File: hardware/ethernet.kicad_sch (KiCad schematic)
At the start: 25 parts, among them J4 HC-RJ45-055-7, U2 TMI7301, U5 SI3404-A-GMR

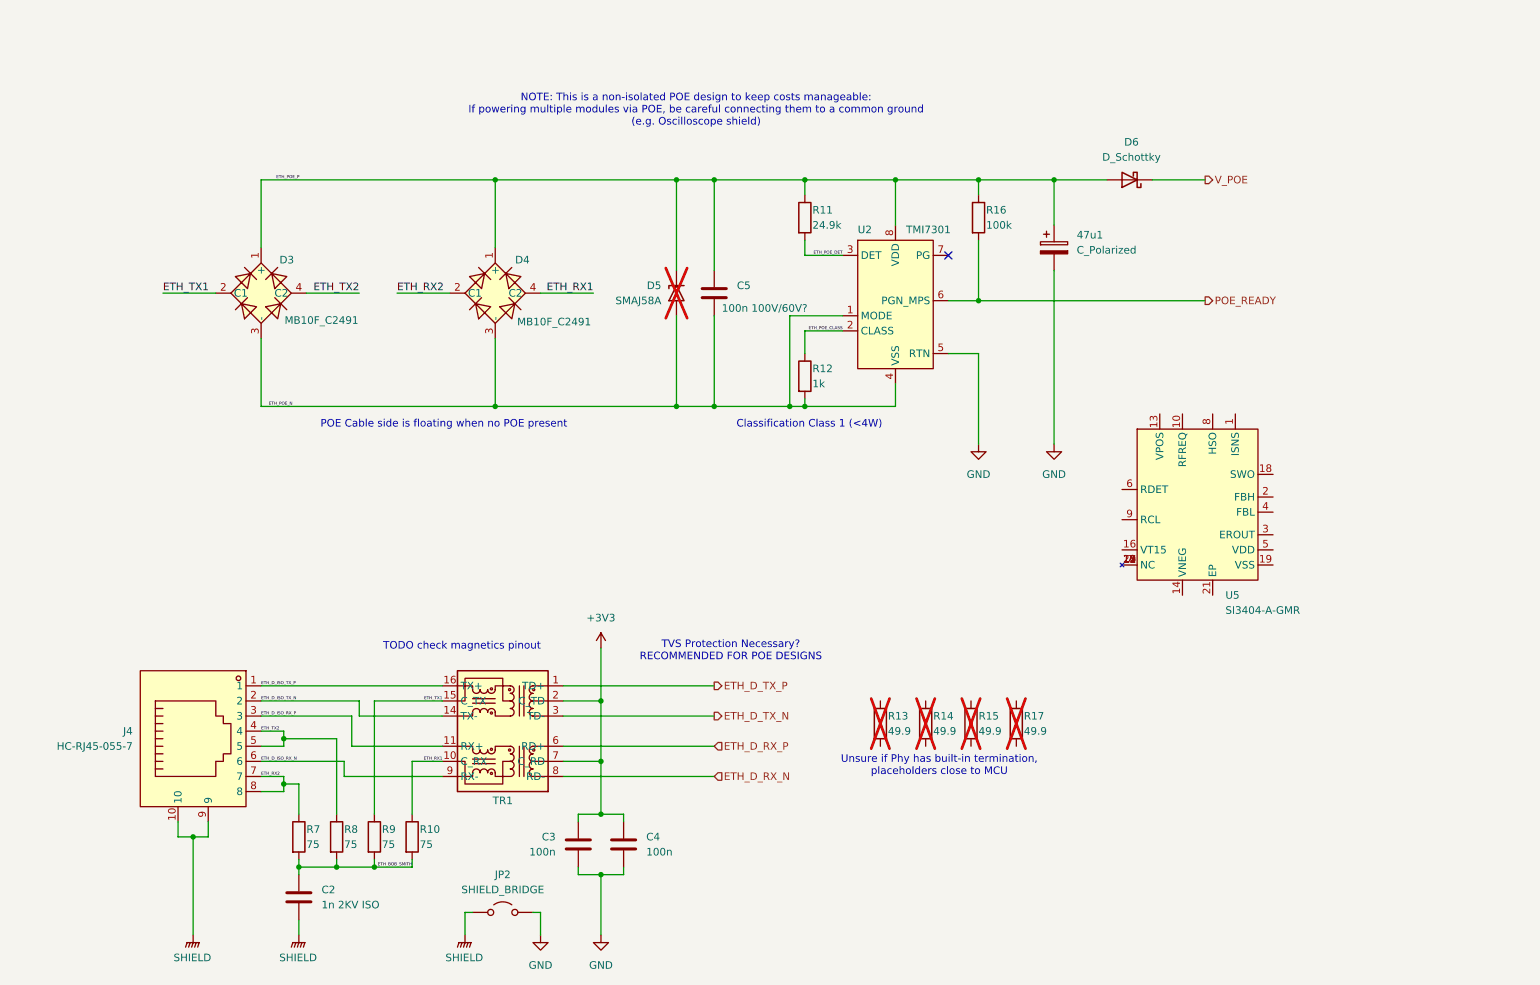
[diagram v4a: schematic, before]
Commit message: Add XTAL, rough POE Schematic
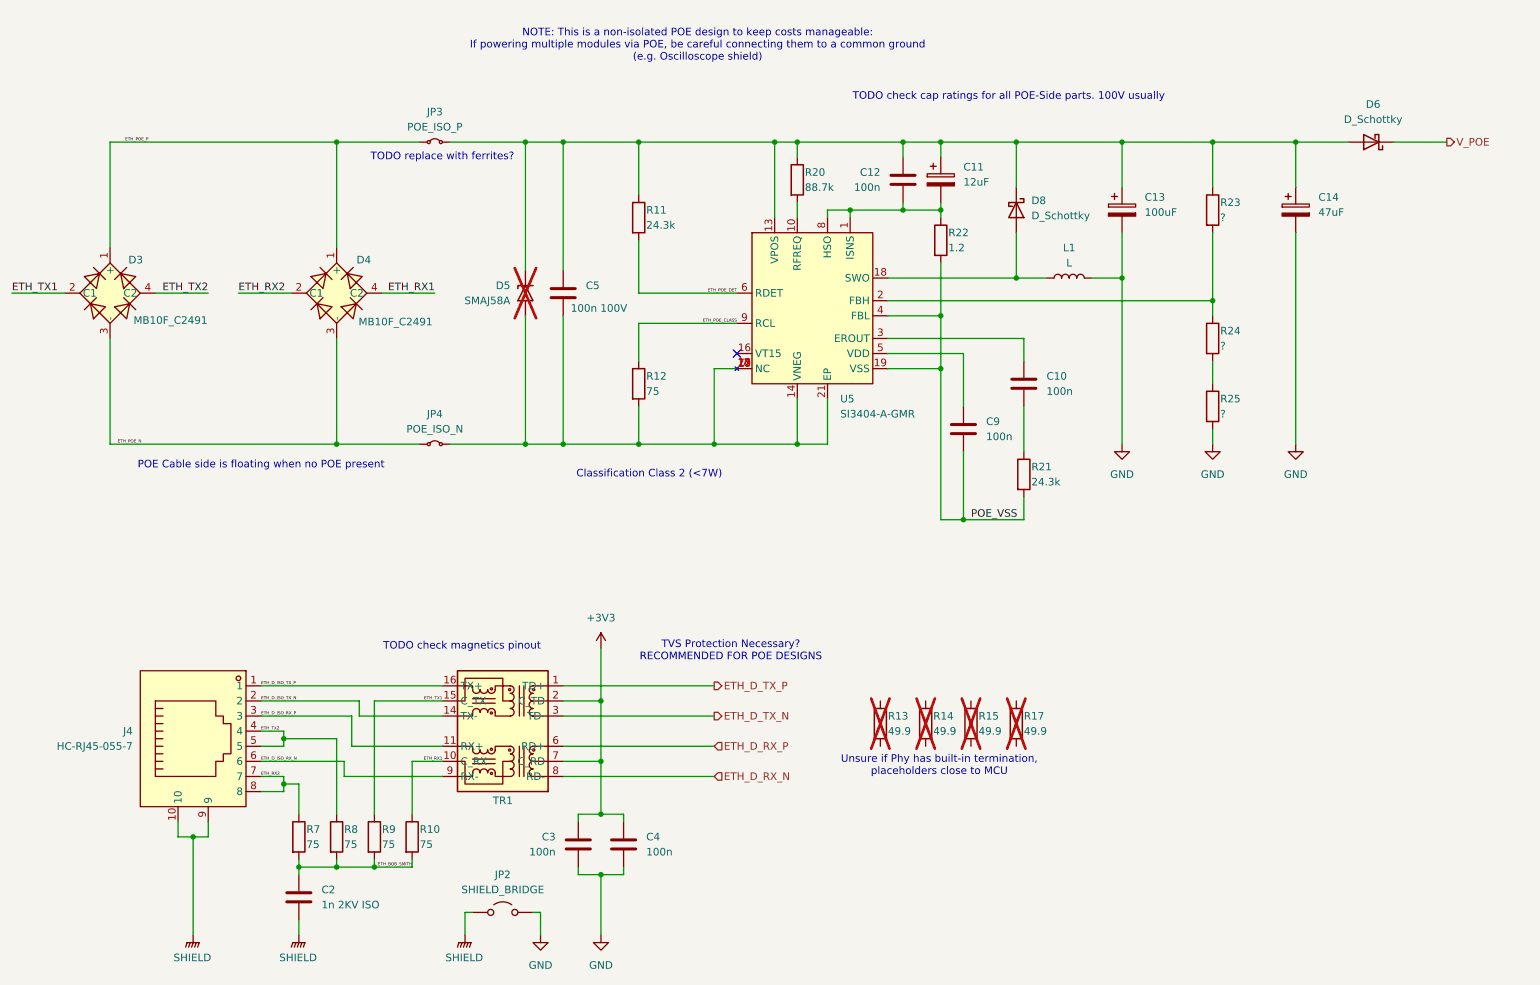
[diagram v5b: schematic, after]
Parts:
- removed R16: 100k, Resistor_SMD:R_0402_1005Metric, symbol Device:R
- removed U2: TMI7301, uPTP:SOP-8_L4.9-W3.9-P1.27-LS6.0-TL, symbol uPTP:TMI7301
- added C10, C12, C9: 100n, Capacitor_SMD:C_0402_1005Metric, symbol Device:C
- added C11: 12uF, symbol Device:C_Polarized
- added C13: 100uF, symbol Device:C_Polarized
- added D8: D_Schottky, symbol Device:D_Schottky
- added JP3: POE_ISO_P, symbol Jumper:Jumper_2_Small_Bridged
- added JP4: POE_ISO_N, symbol Jumper:Jumper_2_Small_Bridged
- added L1: L, symbol Device:L
- added R20: 88.7k, Resistor_SMD:R_0402_1005Metric, symbol Device:R
- added R21: 24.3k, Resistor_SMD:R_0402_1005Metric, symbol Device:R
- added R22: 1.2, Resistor_SMD:R_0402_1005Metric, symbol Device:R
- added R23, R24, R25: ?, Resistor_SMD:R_0402_1005Metric, symbol Device:R
- C14: renamed from 47u1; value C_Polarized -> 47uF
- C5: value 100n 100V/60V? -> 100n 100V
- R11: value 24.9k -> 24.3k
- R12: value 1k -> 75
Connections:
- net ETH_POE_CLASS: now also U5.9 (RCL)
- net ETH_POE_DET: now also U5.6 (RDET)
- net ETH_POE_N: now also JP4.1 (A); no longer C5.2, D5.2 (A2), R12.2
- net ETH_POE_P: now also JP3.1 (A); no longer C14.1, C5.1, D5.1 (A1), D6.2 (A), R11.1
- net GND: now also C13.2, L1.2, R25.2
- net at U5.1 (ISNS): now also U5.8 (HSO), C11.2, C12.2, R22.1
- net at U5.10 (RFREQ): now also R20.2
- net at U5.11 (NC), U5.12 (NC), U5.15 (NC)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: now also C5.2, D5.2 (A2), R12.2, U5.14 (VNEG), U5.21 (EP), JP4.2 (B)
- net at U5.13 (VPOS): now also C14.1, C5.1, D5.1 (A1), D6.2 (A), R11.1, C11.1, C12.1, C13.1, D8.1 (K), JP3.2 (B), R20.1, R23.1
- net at U5.18 (SWO): now also D8.2 (A), L1.1
- net POE_VSS: now reaches U5.19 (VSS)
- net POE_VSS: now also U5.4 (FBL), C9.2, R21.2, R22.2
- net at U5.2 (FBH): now also R23.2, R24.1
- net at U5.3 (EROUT): now also C10.1
- net at U5.5 (VDD): now also C9.1
- new net: R24.2, R25.1
- new net: C10.2, R21.1
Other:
- note added: "Classification Class 2 (<7W)"
- note added: "TODO check cap ratings for all POE-Side parts. 100V usually"
- note added: "TODO replace with ferrites?"
- note removed: "Classification Class 1 (<4W)"
- moved on the sheet: C14, C5, D3, D4, D5, D6, R11, R12, U5

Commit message: Neaten up schematic hierarchy
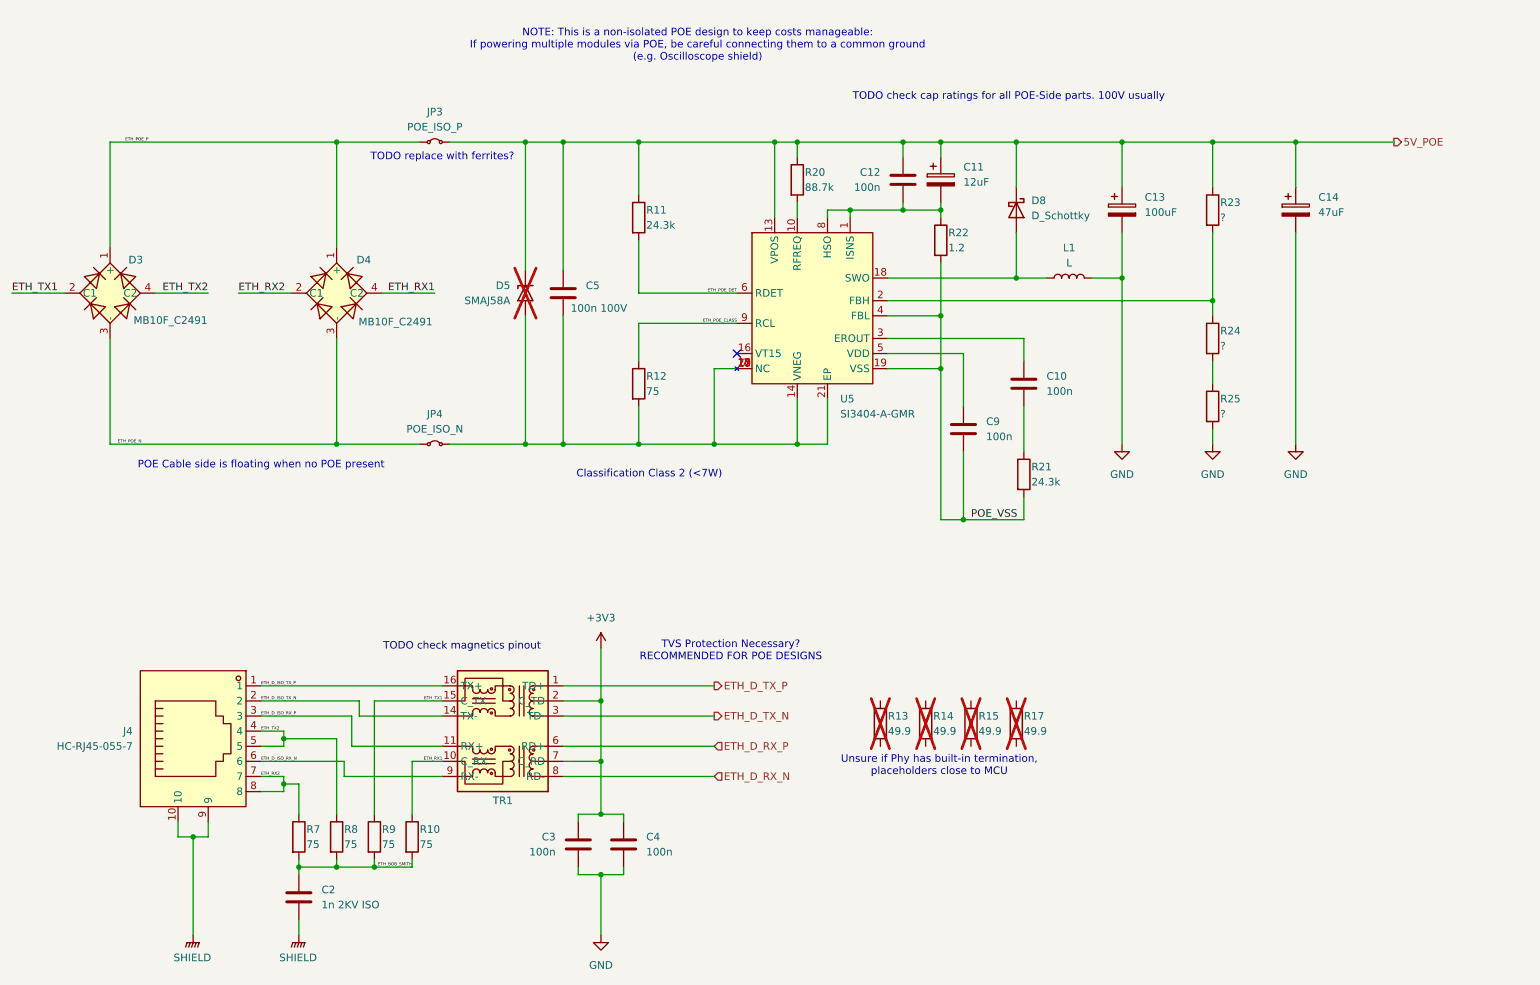
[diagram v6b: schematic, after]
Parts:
- removed D6: D_Schottky, Diode_SMD:D_SOD-323, symbol Device:D_Schottky
- removed JP2: SHIELD_BRIDGE, Jumper:SolderJumper-2_P1.3mm_Open_RoundedPad1.0x1.5mm, symbol Jumper:Jumper_2_Open
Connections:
- net 5V_POE: now reaches C11.1, C12.1, C13.1, C14.1, C5.1, D5.1 (A1), D8.1 (K), JP3.2 (B), R11.1, R20.1, R23.1, U5.13 (VPOS)

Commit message: Confirm all part footprints, start rought layout
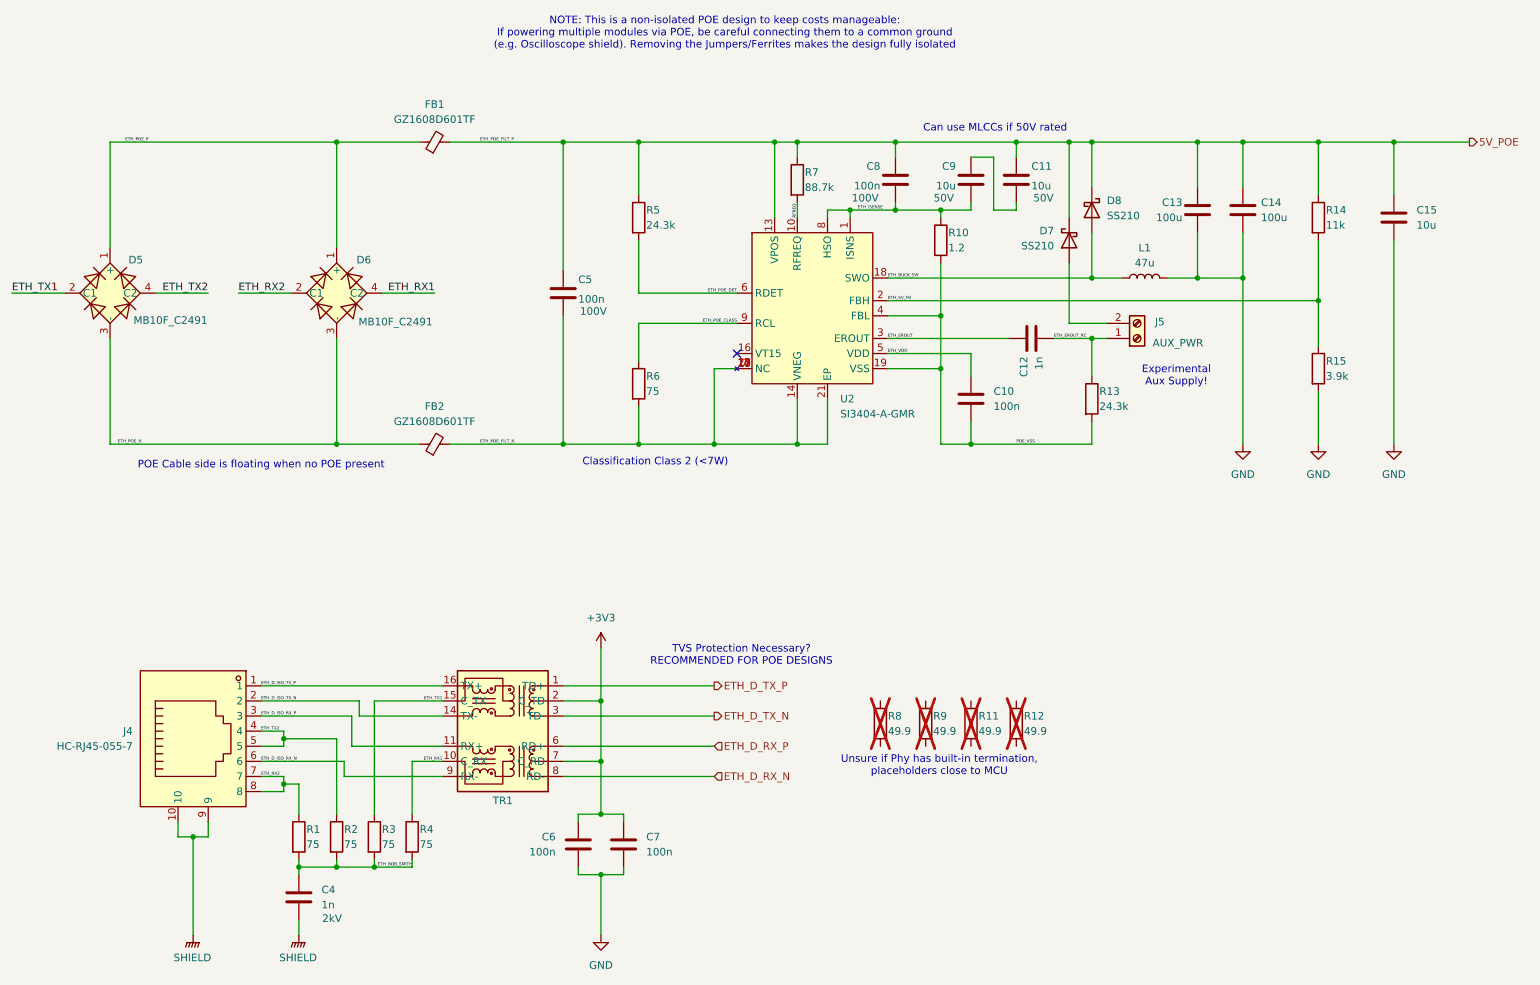
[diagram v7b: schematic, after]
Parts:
- removed C11: 12uF, symbol Device:C_Polarized
- removed C12: 100n, Capacitor_SMD:C_0402_1005Metric, symbol Device:C
- removed C13: 100uF, symbol Device:C_Polarized
- removed C14: 47uF, symbol Device:C_Polarized
- removed D5: SMAJ58A, Diode_SMD:D_SMA, symbol Diode:SMAJ58A
- removed JP3: POE_ISO_P, symbol Jumper:Jumper_2_Small_Bridged
- removed JP4: POE_ISO_N, symbol Jumper:Jumper_2_Small_Bridged
- removed R25: ?, Resistor_SMD:R_0402_1005Metric, symbol Device:R
- added C11, C9: 10u, Capacitor_SMD:C_0805_2012Metric, symbol Device:C
- added C13, C14: 100u, Capacitor_SMD:C_1206_3216Metric, symbol Device:C
- added C15: 10u, Capacitor_SMD:C_0603_1608Metric, symbol Device:C
- added C8: 100n, Capacitor_SMD:C_0805_2012Metric, symbol Device:C
- added D7: SS210, Diode_SMD:D_SMA, symbol Device:D_Schottky
- added FB1, FB2: GZ1608D601TF, Resistor_SMD:R_0603_1608Metric, symbol Device:FerriteBead_Small
- added J5: AUX_PWR, TerminalBlock_Phoenix:TerminalBlock_Phoenix_MPT-0,5-2-2.54_1x02_P2.54mm_Horizontal, symbol Connector:Screw_Terminal_01x02
- C12: renamed from C10; value 100n -> 1n
- C4: renamed from C2; value 1n 2KV ISO -> 1n; footprint (none) -> Capacitor_SMD:C_1206_3216Metric; LCSC Part (none) -> C9196
- C5: value 100n 100V -> 100n; LCSC Part (none) -> C28233
- D8: value D_Schottky -> SS210; footprint (none) -> Diode_SMD:D_SMA; LCSC Part (none) -> C14996
- L1: value L -> 47u; footprint (none) -> Inductor_SMD:L_Changjiang_FXL0630; LCSC Part (none) -> C475913
- R14: renamed from R23; value ? -> 11k
- R15: renamed from R24; value ? -> 3.9k
- renumbered C9 to C10, C3 to C6, C4 to C7, D3 to D5, D4 to D6, R7 to R1, R22 to R10, R15 to R11, R17 to R12, R21 to R13, R8 to R2, R9 to R3, R10 to R4, R11 to R5, R12 to R6, R20 to R7, R13 to R8, R14 to R9, U5 to U2
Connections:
- net 5V_POE: now also C11.1, C13.1, C14.1, C15.1, C8.1, D7.1 (K), FB1.2
- net ETH_POE_N: now also FB2.1
- net ETH_POE_P: now also FB1.1
- net GND: now also R15.2, C13.2, C14.2, C15.2
- net ETH_ISENSE: now reaches R10.1, U2.1 (ISNS), U2.8 (HSO)
- net ETH_ISENSE: now also C8.2, C9.2
- net ETH_POE_FILT_N: now reaches C5.2, R6.2, U2.11 (NC), U2.12 (NC), U2.14 (VNEG), U2.15 (NC), U2.17 (NC), U2.20 (NC), U2.21 (EP), U2.7 (NC)
- net ETH_POE_FILT_N: now also FB2.2
- net ETH_BUCK_SW: now reaches D8.2 (A), L1.1, U2.18 (SWO)
- net ETH_EROUT_RC: now reaches C12.2, R13.1
- net ETH_EROUT_RC: now also J5.1 (Pin_1)
- net ETH_5V_FB: now reaches R14.2, R15.1, U2.2 (FBH)
- net ETH_EROUT: now reaches C12.1, U2.3 (EROUT)
- net ETH_VDD: now reaches C10.1, U2.5 (VDD)
- net RFREQ: now reaches R7.2, U2.10 (RFREQ)
- new net: C11.2, C9.1
- new net: D7.2 (A), J5.2 (Pin_2)
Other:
- note added: "Can use MLCCs if 50V rated"
- note added: "Experimental Aux Supply!"
- note added: "NOTE: This is a non-isolated POE design to keep costs manageable: If powering multiple modules via POE, be careful connecting them to a common ground (e.g. Oscilloscope shield). Removing the Jumpers/Ferrites makes the design fully isolated"
- note removed: "NOTE: This is a non-isolated POE design to keep costs manageable: If powering multiple modules via POE, be careful connecting them to a common ground (e.g. Oscilloscope shield)"
- note removed: "TODO check cap ratings for all POE-Side parts. 100V usually"
- note removed: "TODO check magnetics pinout"
- note removed: "TODO replace with ferrites?"
- moved on the sheet: C10, C12, D8, L1, R13, R14, R15

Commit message: Tidy up layout
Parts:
- renumbered J4 to J5, J5 to J6
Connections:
- net ETH_AUX: now reaches D7.2 (A), J6.2 (Pin_2)
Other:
- note added: "More test points?"
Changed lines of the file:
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@@
 		)
 	)
+	(text "More test points?"
+		(exclude_from_sim no)
+		(at 191.262 106.426 0)
+		(effects
+			(font
+				(size 1.27 1.27)
+			)
+		)
+	)
 	(text "NOTE: This is a non-isolated POE design to keep costs manageable:\nIf powering multiple modules via POE, be careful connecting them to a common ground\n(e.g. Oscilloscope shield). Removing the Jumpers/Ferrites makes the design fully isolated"
 		(exclude_from_sim no)
@@
 		)
 	)
+	(label "ETH_AUX"
+		(at 199.39 68.58 0)
+		(effects
+			(font
+				(size 0.508 0.508)
+				(color 132 132 132 1)
+			)
+			(justify left bottom)
+		)
+	)
 	(label "ETH_TX1"
 		(at 93.98 132.08 180)
@@
 		(dnp no)
 		(fields_autoplaced yes)
-		(property "Reference" "#PWR016"
+		(property "Reference" "#PWR017"
 			(at 69.85 176.53 0)
 			(effects
@@
 			(project "uPTP"
 				(path "/c29659fd-9e8d-4714-a690-4e74e6e849c2/8e64a963-7181-4c69-8059-c99395347002"
-					(reference "#PWR016")
+					(reference "#PWR017")
 					(unit 1)
 				)
@@
 		(dnp no)
 		(fields_autoplaced yes)
-		(property "Reference" "#PWR015"
+		(property "Reference" "#PWR016"
 			(at 52.07 176.53 0)
 			(effects
@@
 			(project ""
 				(path "/c29659fd-9e8d-4714-a690-4e74e6e849c2/8e64a963-7181-4c69-8059-c99395347002"
-					(reference "#PWR015")
+					(reference "#PWR016")
 					(unit 1)
 				)
@@
 		(dnp no)
 		(fields_autoplaced yes)
-		(property "Reference" "#PWR021"
+		(property "Reference" "#PWR022"
 			(at 254 95.25 0)
 			(effects
@@
 			(project "uPTP"
 				(path "/c29659fd-9e8d-4714-a690-4e74e6e849c2/8e64a963-7181-4c69-8059-c99395347002"
-					(reference "#PWR021")
+					(reference "#PWR022")
 					(unit 1)
 				)
@@
 		(dnp no)
 		(fields_autoplaced yes)
-		(property "Reference" "#PWR020"
+		(property "Reference" "#PWR021"
 			(at 241.3 95.25 0)
 			(effects
@@
 			(project "uPTP"
 				(path "/c29659fd-9e8d-4714-a690-4e74e6e849c2/8e64a963-7181-4c69-8059-c99395347002"
-					(reference "#PWR020")
+					(reference "#PWR021")
 					(unit 1)
 				)
@@
 		(on_board yes)
 		(dnp no)
-		(property "Reference" "J5"
+		(property "Reference" "J6"
 			(at 214.63 68.326 0)
 			(effects
@@
 			(project "uPTP"
 				(path "/c29659fd-9e8d-4714-a690-4e74e6e849c2/8e64a963-7181-4c69-8059-c99395347002"
-					(reference "J5")
+					(reference "J6")
 					(unit 1)
 				)
@@
 		(dnp no)
 		(fields_autoplaced yes)
-		(property "Reference" "#PWR018"
+		(property "Reference" "#PWR019"
 			(at 120.65 177.8 0)
 			(effects
@@
 			(project ""
 				(path "/c29659fd-9e8d-4714-a690-4e74e6e849c2/8e64a963-7181-4c69-8059-c99395347002"
-					(reference "#PWR018")
+					(reference "#PWR019")
 					(unit 1)
 				)
@@
 		(dnp no)
 		(fields_autoplaced yes)
-		(property "Reference" "#PWR019"
+		(property "Reference" "#PWR020"
 			(at 228.6 95.25 0)
 			(effects
@@
 			(project "uPTP"
 				(path "/c29659fd-9e8d-4714-a690-4e74e6e849c2/8e64a963-7181-4c69-8059-c99395347002"
-					(reference "#PWR019")
+					(reference "#PWR020")
 					(unit 1)
 				)
@@
 		(on_board yes)
 		(dnp no)
-		(property "Reference" "J4"
+		(property "Reference" "J5"
 			(at 41.91 137.1599 0)
 			(effects
@@
 			(project "uPTP"
 				(path "/c29659fd-9e8d-4714-a690-4e74e6e849c2/8e64a963-7181-4c69-8059-c99395347002"
-					(reference "J4")
+					(reference "J5")
 					(unit 1)
 				)
@@
 		(dnp no)
 		(fields_autoplaced yes)
-		(property "Reference" "#PWR017"
+		(property "Reference" "#PWR018"
 			(at 120.65 127 0)
 			(effects
@@
 			(project ""
 				(path "/c29659fd-9e8d-4714-a690-4e74e6e849c2/8e64a963-7181-4c69-8059-c99395347002"
-					(reference "#PWR017")
+					(reference "#PWR018")
 					(unit 1)
 				)
